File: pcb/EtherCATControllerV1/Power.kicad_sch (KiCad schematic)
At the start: 64 parts, among them U2 TPS54360DDAR, U3 LDL1117S33R, U4 LP5907MFX-3.3_NOPB, U8 LM76005RNPR

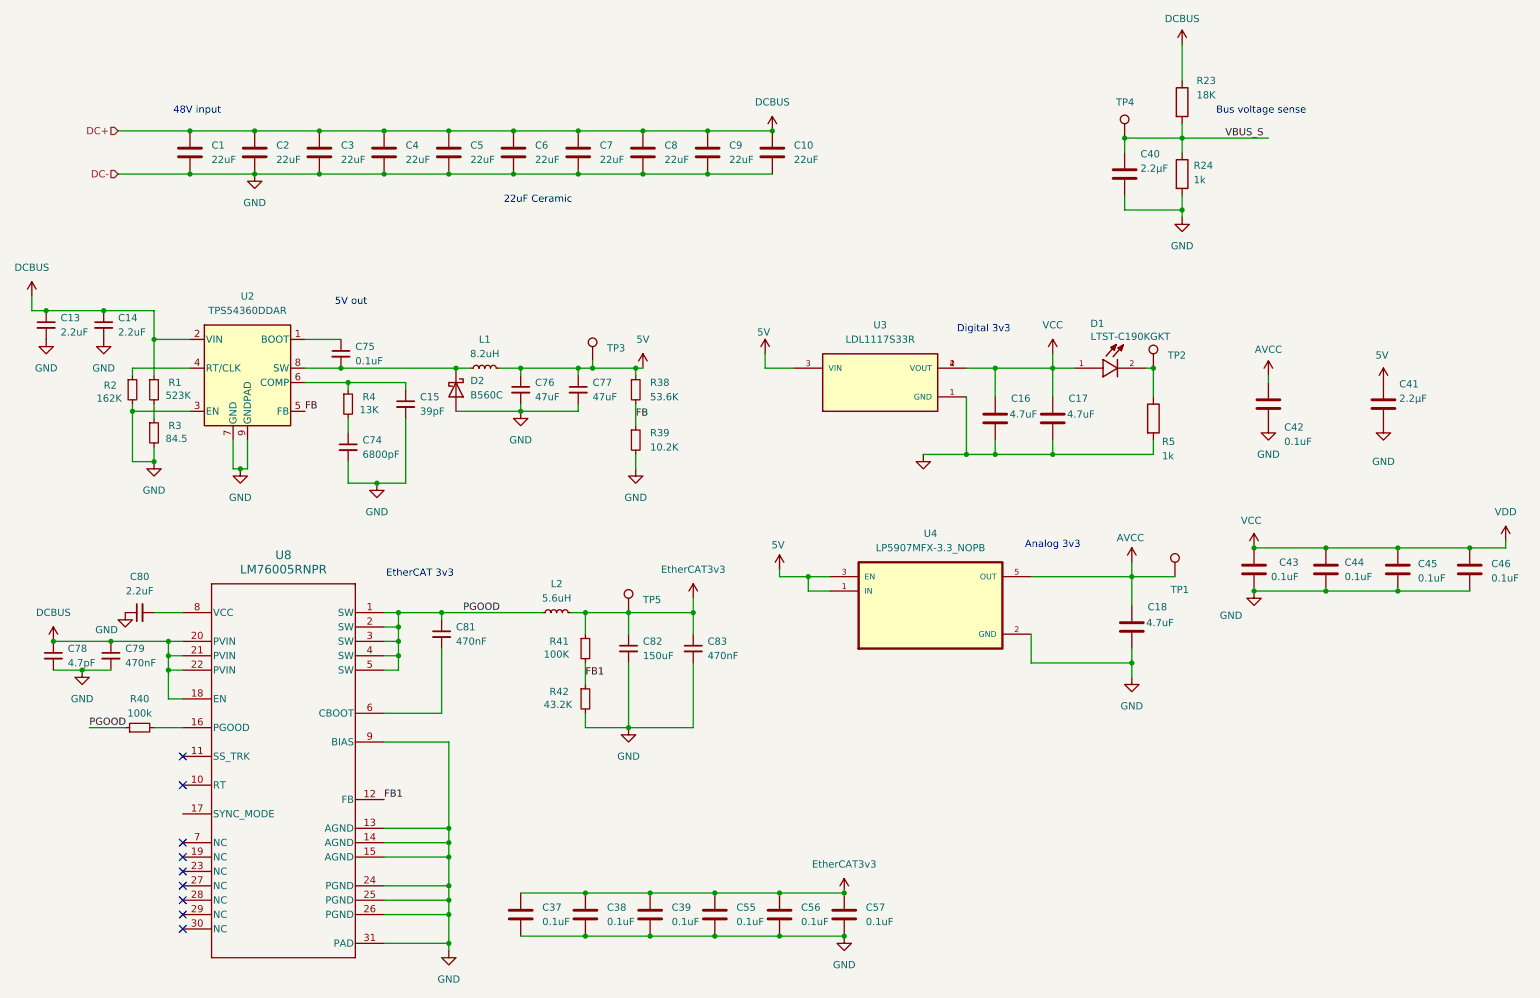
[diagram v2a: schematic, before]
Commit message: schematic finished, need to set proper ERCs
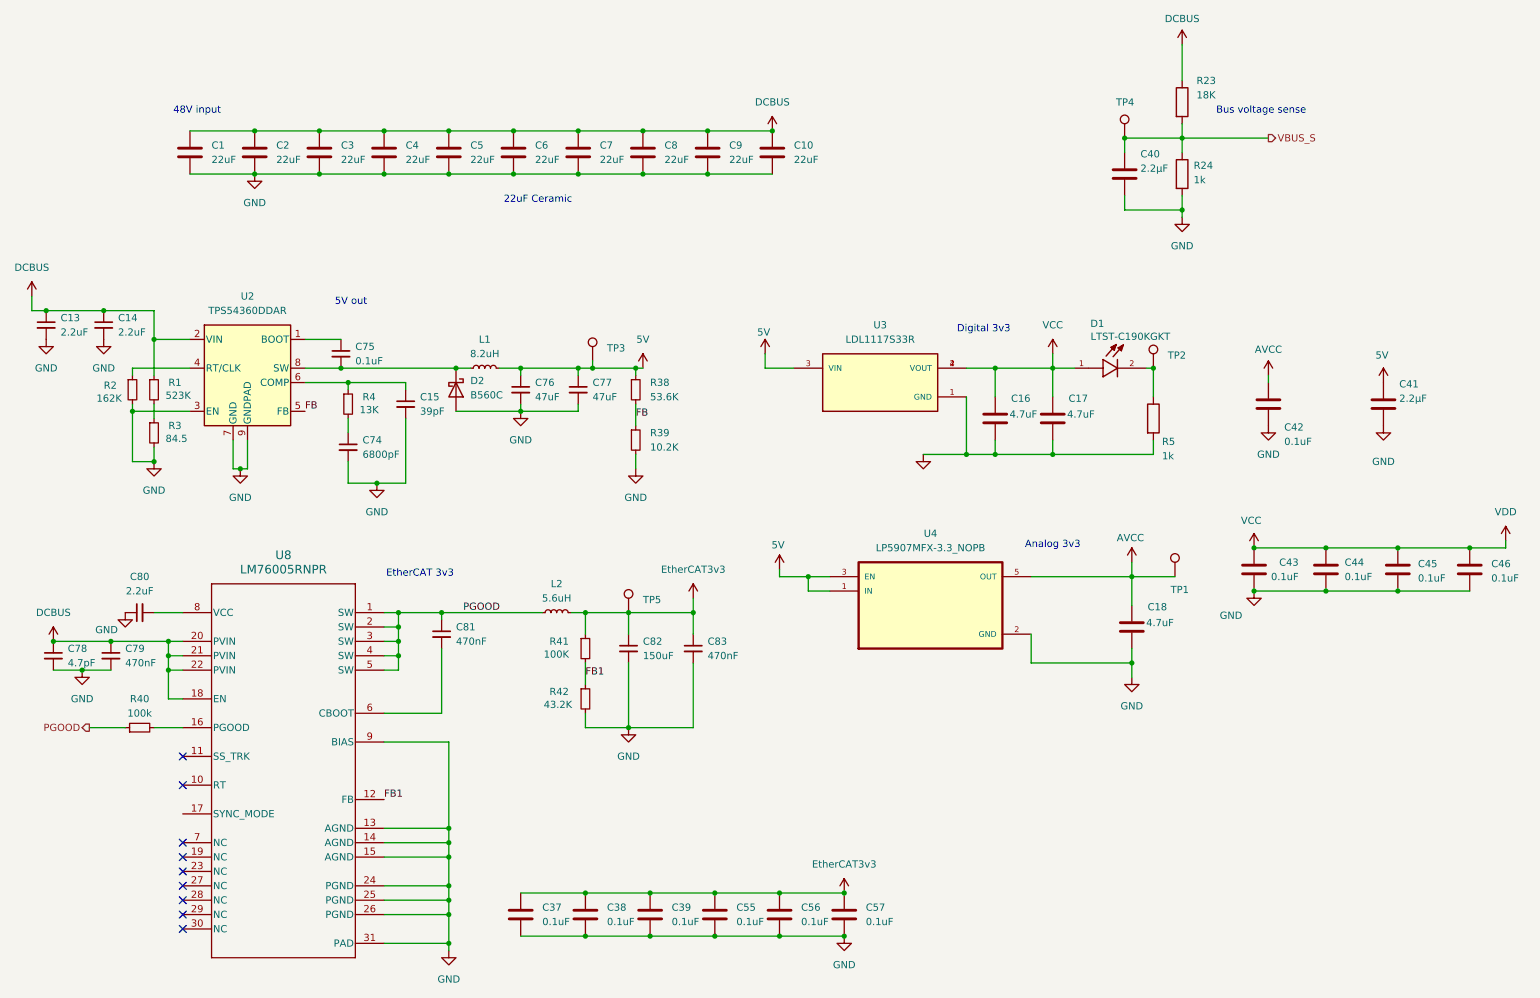
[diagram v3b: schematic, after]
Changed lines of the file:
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@@
-	)
-	(junction
-		(at 48.26 39.37)
-		(diameter 0)
-		(color 0 0 0 0)
 	)
 	(junction
@@
 	(junction
 		(at 93.98 182.88)
-		(diameter 0)
-		(color 0 0 0 0)
-	)
-	(junction
-		(at 48.26 46.99)
 		(diameter 0)
 		(color 0 0 0 0)
@@
 	(wire
 		(pts
-			(xy 35.56 46.99) (xy 48.26 46.99)
-		)
-		(stroke
-			(width 0)
-			(type default)
-		)
-	)
-	(wire
-		(pts
 			(xy 102.87 81.28) (xy 106.68 81.28)
 		)
@@
 		(pts
 			(xy 152.4 118.11) (xy 157.48 118.11)
-		)
-		(stroke
-			(width 0)
-			(type default)
-		)
-	)
-	(wire
-		(pts
-			(xy 35.56 39.37) (xy 48.26 39.37)
 		)
 		(stroke
@@
 				(size 1.27 1.27)
 			)
-		)
-	)
-	(label "VBUS_S"
-		(at 231.14 40.64 0)
-		(fields_autoplaced yes)
-		(effects
-			(font
-				(size 1.27 1.27)
-			)
-			(justify left bottom)
 		)
 	)
@@
 		)
 	)
-	(label "PGOOD"
-		(at 30.48 144.78 0)
-		(fields_autoplaced yes)
-		(effects
-			(font
-				(size 1.27 1.27)
-			)
-			(justify left bottom)
-		)
-	)
 	(label "FB"
 		(at 127 90.17 0)
@@
 		)
 	)
-	(hierarchical_label "DC-"
-		(shape input)
-		(at 35.56 46.99 180)
+	(hierarchical_label "PGOOD"
+		(shape output)
+		(at 30.48 144.78 180)
 		(fields_autoplaced yes)
 		(effects
@@
 		)
 	)
-	(hierarchical_label "DC+"
-		(shape input)
-		(at 35.56 39.37 180)
+	(hierarchical_label "VBUS_S"
+		(shape output)
+		(at 238.76 40.64 0)
 		(fields_autoplaced yes)
 		(effects
@@
 				(size 1.27 1.27)
 			)
-			(justify right)
-		)
-	)
+			(justify left)
+		)
+	)

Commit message: fix all ERCs
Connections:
- net GND: now also U8.17 (SYNC_MODE)

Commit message: Added more BOM items
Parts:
- removed C10, C5, C6, C9: 22uF, symbol Device:C
- C1, C2, C3, C4: value 22uF -> 10uF; LCSC Part Number C784103 -> C153035
- C40: value ${CAPACITANCE} -> 2.2uF
- C7, C8: LCSC Part Number C784103 -> C1921234
- U3: LCSC Part Number (none) -> C435835
- U4: LCSC Part Number (none) -> C80670
- U8: LCSC Part Number (none) -> C2866241
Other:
- note added: "22uF Stacked Ceramic Bypass 10uF bypasses Bulk Caps on IO Board"
- note removed: "22uF Ceramic"
- moved on the sheet: C7, C8
